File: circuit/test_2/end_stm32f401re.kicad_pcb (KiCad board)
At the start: 2 copper layers, 70 x 55.8 mm, 37 parts, among them J1 Micro_SD_Card_Det, J2 USB_B_Micro, U1 MAX98357_DAC, U2 STM32F401RETx, U3 AMS1117-3.3

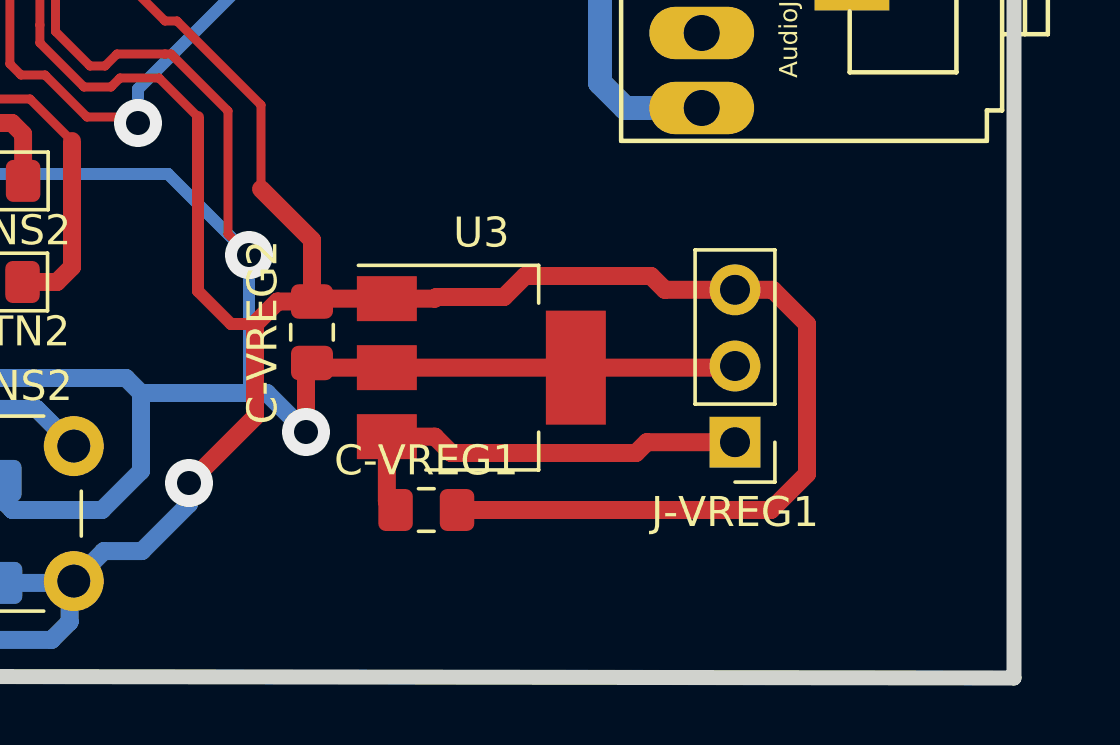
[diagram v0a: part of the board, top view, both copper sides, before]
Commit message: add diode on power reg
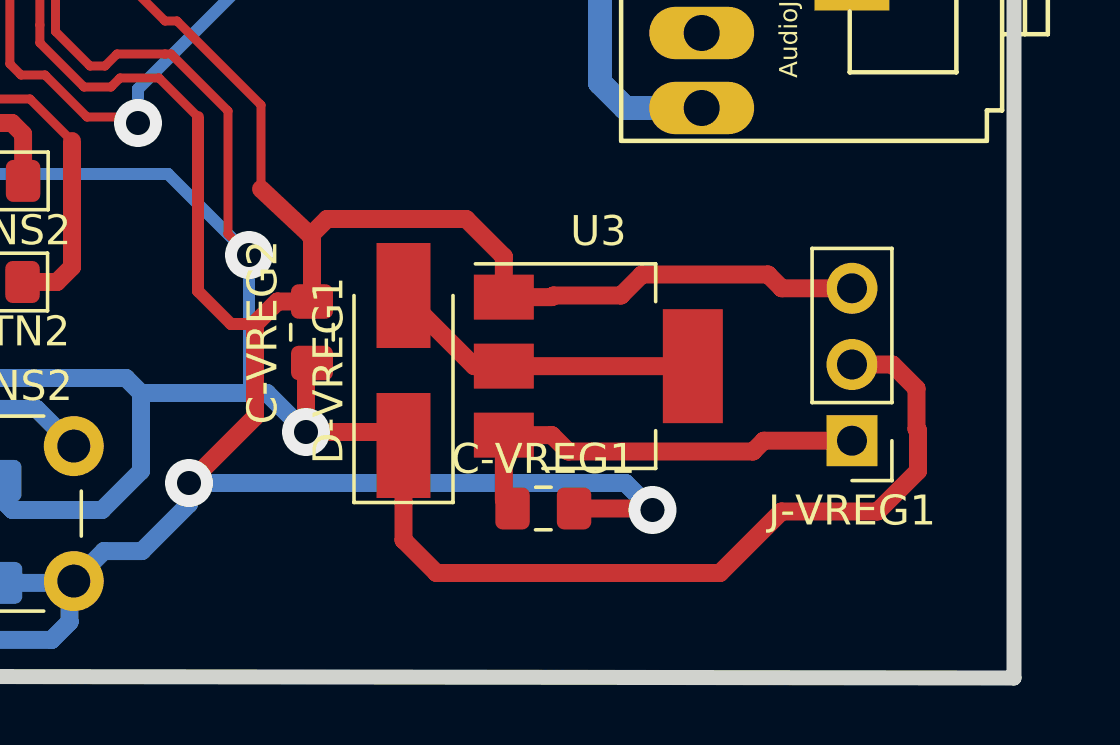
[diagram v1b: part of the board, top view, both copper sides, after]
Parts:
- added D-VREG1: D, Diode_SMD:D_SMA_Handsoldering, F.Cu at (117.7, 80.5)
- moved C-VREG1 3.90 mm to (122.3, 85.2)
- moved J-VREG1 3.90 mm to (132.6, 82.9)
- moved U3 3.90 mm to (124.1, 80.4)
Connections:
- U3 pad 2: VDD -> Net-(D-VREG1-Pad2)
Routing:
- net VDD: track 296.0 -> 313.8 mm
- net Net-(D-VREG1-Pad2): track 0.00 -> 11.5 mm
- net GND: track 413.4 -> 417.9 mm, vias 4 -> 5

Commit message: RESET to START
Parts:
- removed SW-RST1: SW_Push, Button_Switch_THT:SW_PUSH_6mm
- added C-START1: C, Capacitor_SMD:C_0805_2012Metric_Pad1.15x1.40mm_HandSolder, B.Cu at (74.3, 56.4)
- added R-START1: 10K, Resistor_SMD:R_0805_2012Metric_Pad1.15x1.40mm_HandSolder, B.Cu at (74.3, 58.6)
- added SW-START1: SW_Push, Button_Switch_THT:SW_PUSH_6mm, F.Cu at (77.4, 59.6)
- moved R-RST1 33.9 mm to (104.5, 42.1), turned to 90 degrees
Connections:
- U2 pad 2: Net-(U2-Pad2) -> /BTN_START
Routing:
- net /BTN_START: track 0.00 -> 34.2 mm, vias 0 -> 1
- net /NRST: track 69.3 -> 55.0 mm
- net GND: track 417.9 -> 420.0 mm
- net VDD: track 313.8 -> 315.4 mm
